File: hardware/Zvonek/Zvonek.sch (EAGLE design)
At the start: 34 parts, among them J1 J25MM, K1 ARK500/3, T1 BC847, T2 BC847, T3 BC847, T4 BC847, T5 IRF9530

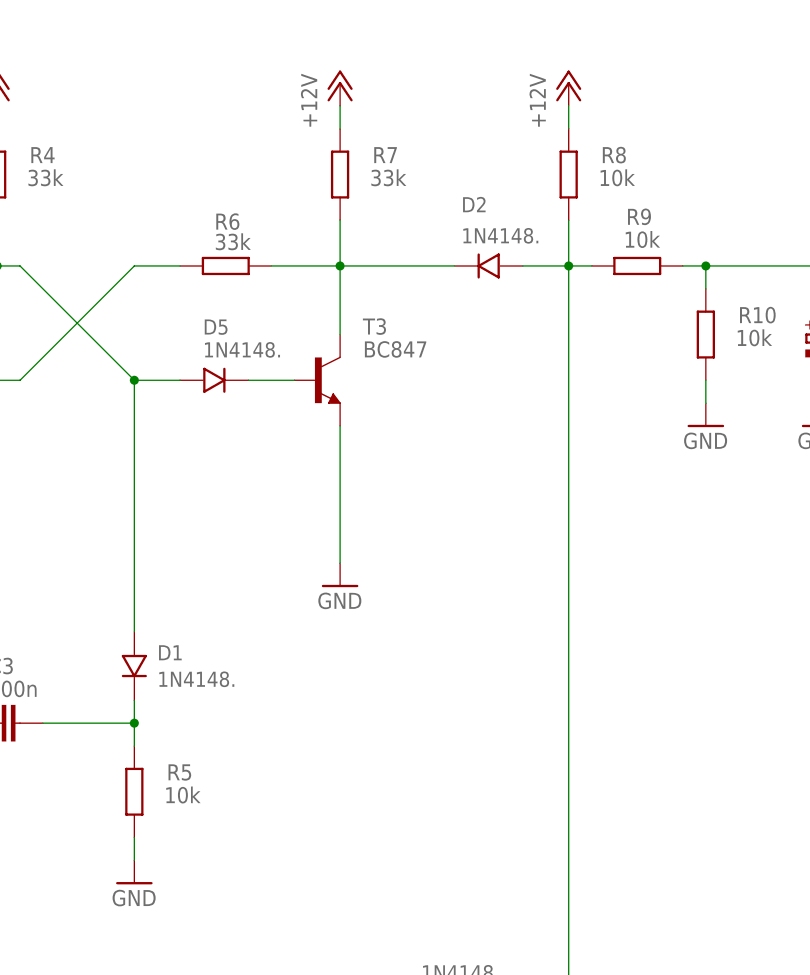
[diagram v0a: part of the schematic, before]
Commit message: Change some component values
This version matches the board that was manufactured.
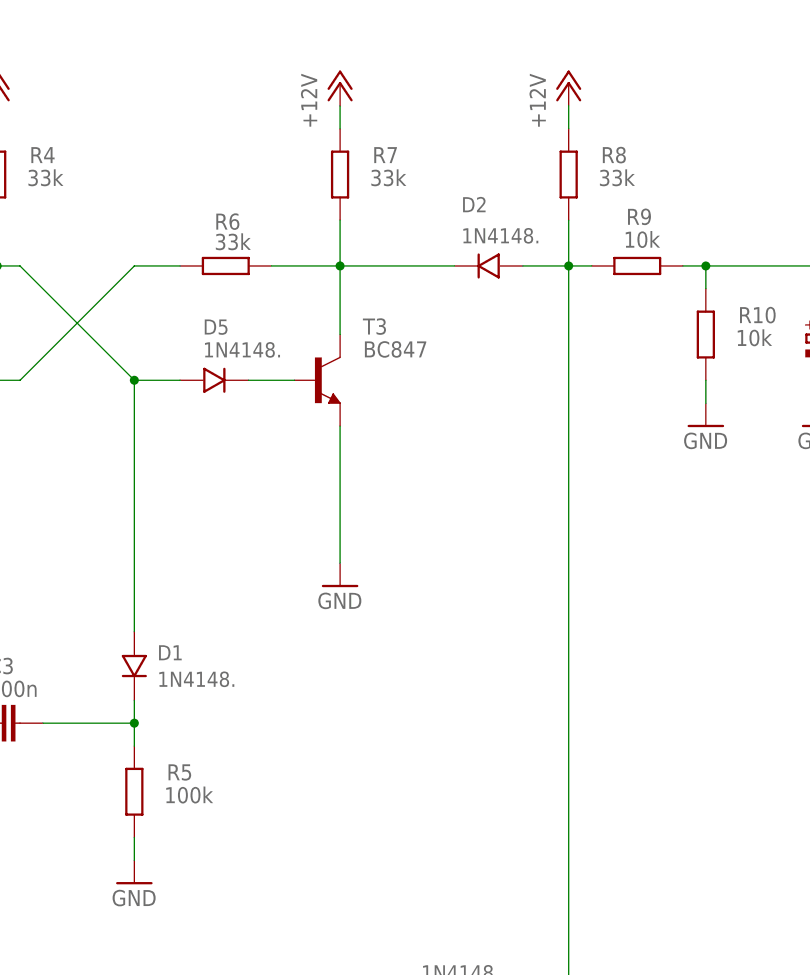
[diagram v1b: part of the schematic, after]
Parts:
- R5: value 10k -> 100k
- R8: value 10k -> 33k
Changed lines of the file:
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@@
 <part name="R4" library="rcl" library_urn="urn:adsk.eagle:library:334" deviceset="R-EU_" device="R1206" package3d_urn="urn:adsk.eagle:package:23540/2" value="33k"/>
 <part name="R7" library="rcl" library_urn="urn:adsk.eagle:library:334" deviceset="R-EU_" device="R1206" package3d_urn="urn:adsk.eagle:package:23540/2" value="33k"/>
-<part name="R8" library="rcl" library_urn="urn:adsk.eagle:library:334" deviceset="R-EU_" device="R1206" package3d_urn="urn:adsk.eagle:package:23540/2" value="10k"/>
+<part name="R8" library="rcl" library_urn="urn:adsk.eagle:library:334" deviceset="R-EU_" device="R1206" package3d_urn="urn:adsk.eagle:package:23540/2" value="33k"/>
 <part name="C2" library="rcl" library_urn="urn:adsk.eagle:library:334" deviceset="CPOL-EU" device="E2.5-6" package3d_urn="urn:adsk.eagle:package:23349/1" value="47u"/>
 <part name="D2" library="#PaJa_31_Edit" deviceset="1N4148" device="."/>
 <part name="D3" library="#PaJa_31_Edit" deviceset="1N4148" device="."/>
 <part name="D1" library="#PaJa_31_Edit" deviceset="1N4148" device="."/>
-<part name="R5" library="rcl" library_urn="urn:adsk.eagle:library:334" deviceset="R-EU_" device="R1206" package3d_urn="urn:adsk.eagle:package:23540/2" value="10k"/>
+<part name="R5" library="rcl" library_urn="urn:adsk.eagle:library:334" deviceset="R-EU_" device="R1206" package3d_urn="urn:adsk.eagle:package:23540/2" value="100k"/>
 <part name="GND3" library="supply1" library_urn="urn:adsk.eagle:library:371" deviceset="GND" device=""/>
 <part name="C3" library="rcl" library_urn="urn:adsk.eagle:library:334" deviceset="C-EU" device="C1206" package3d_urn="urn:adsk.eagle:package:23618/2" value="100n"/>
